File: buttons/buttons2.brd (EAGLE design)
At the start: 69 x 44 mm, 14 parts, among them U1 attiny2313

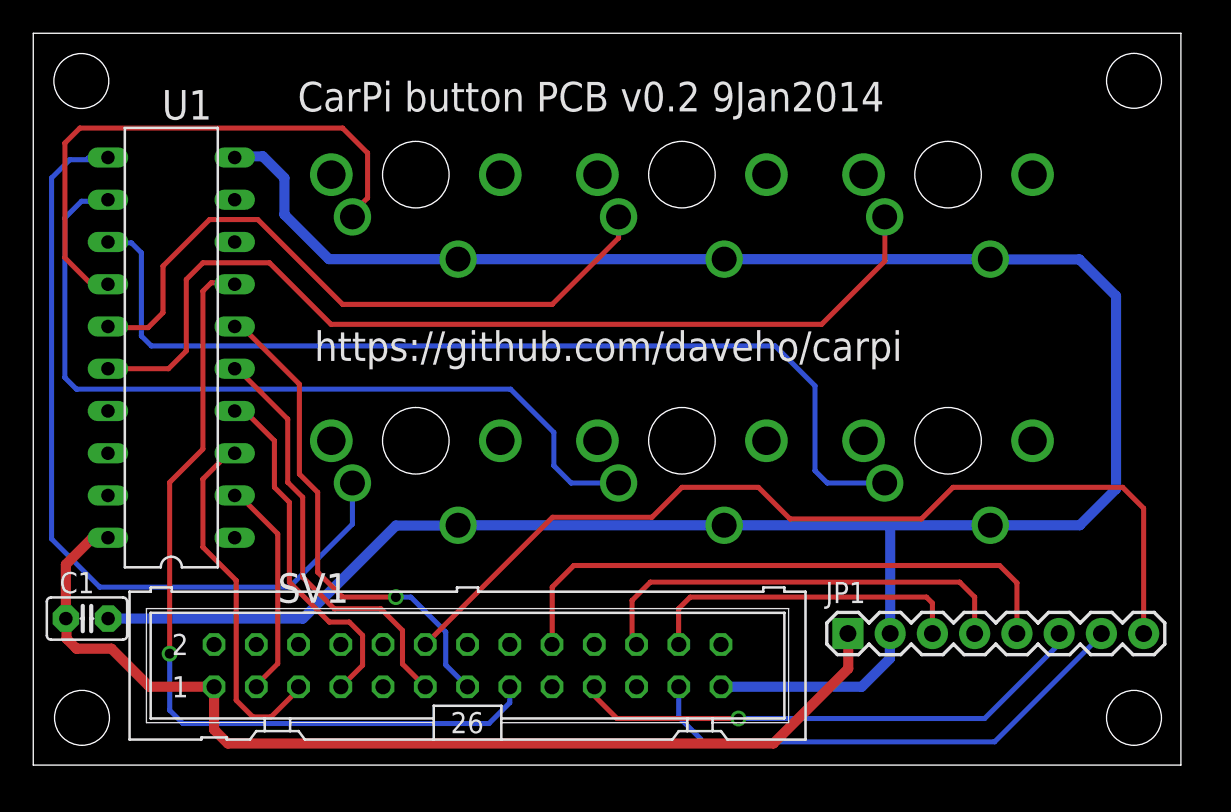
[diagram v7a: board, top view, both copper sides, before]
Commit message: moved buttons: keycaps are 18mm x 18mm
I think everything will still fit, but unfortunately
everything must be routed again...
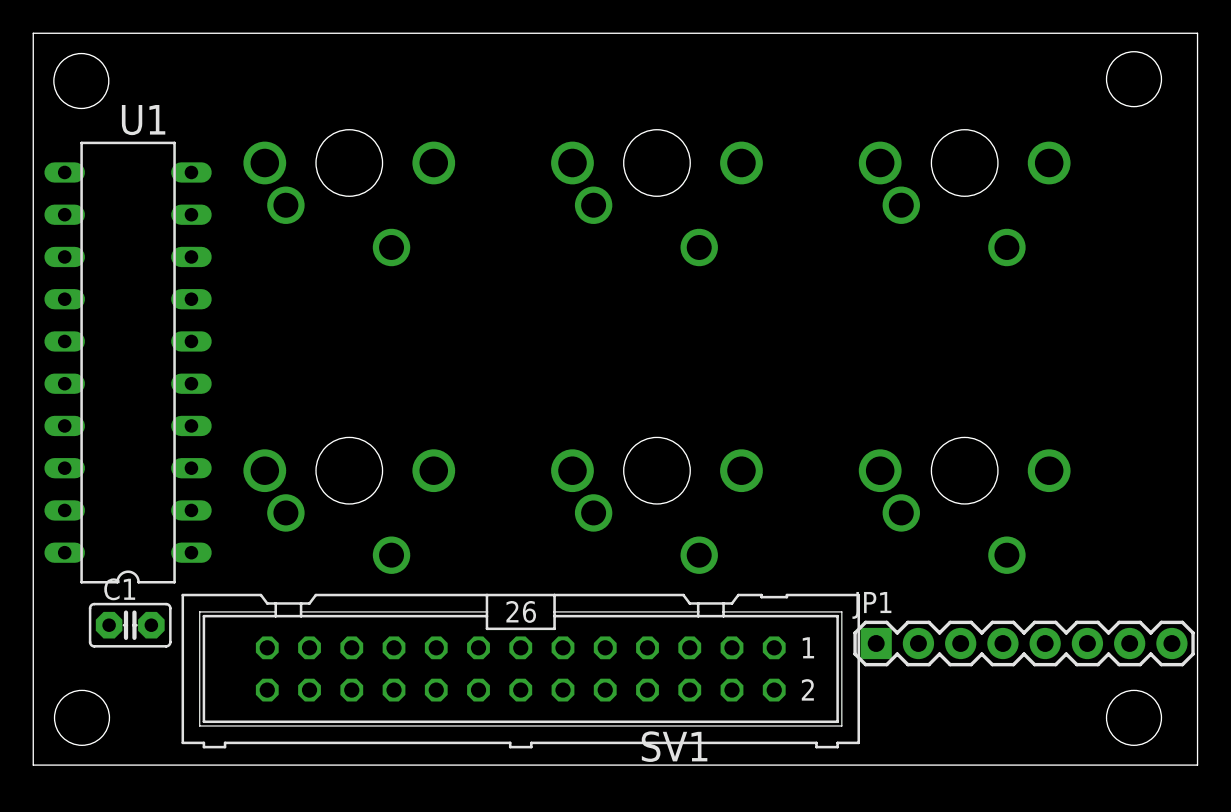
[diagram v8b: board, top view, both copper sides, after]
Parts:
- moved S1 4.39 mm to (19.0, 17.7)
- moved S4 4.06 mm to (19.0, 36.2)
- moved SV1 3.21 mm to (29.3, 5.78), turned to 180 degrees
- moved U1 2.75 mm to (5.70, 24.2)
- moved C1 2.63 mm to (5.83, 8.41)
- moved S2 2.34 mm to (37.5, 17.7)
- moved S3 2.06 mm to (56.0, 17.7)
- moved JP1 1.80 mm to (50.7, 7.31)
- moved S5 1.66 mm to (37.5, 36.2)
- moved S6 1.22 mm to (56.0, 36.2)
- moved STANDOFF3 0.10 mm to (66.2, 41.2)
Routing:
- net GND: track 152.1 -> 0.00 mm
- net VCC: track 62.8 -> 0.00 mm
- net N$4: track 58.6 -> 0.00 mm
- net N$1: track 57.6 -> 0.00 mm
- net LED: track 56.7 -> 0.00 mm
- net BUTTON6: track 50.4 -> 0.00 mm, vias 1 -> 0
- net N$5: track 49.7 -> 0.00 mm
- net N$6: track 49.0 -> 0.00 mm
- net N$2: track 40.1 -> 0.00 mm
- net DC: track 35.4 -> 0.00 mm
- net N$3: track 33.6 -> 0.00 mm
- net MOSI: track 31.6 -> 0.00 mm, vias 1 -> 0
- net SCK: track 30.6 -> 0.00 mm
- net BUTTON5: track 30.1 -> 0.00 mm, vias 1 -> 0
- net RESET: track 26.4 -> 0.00 mm
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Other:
- board size 69 x 44 mm -> 70 x 44 mm
- board text removed: "CarPi button PCB v0.2 9Jan2014"
- board text removed: "https://github.com/daveho/carpi"
